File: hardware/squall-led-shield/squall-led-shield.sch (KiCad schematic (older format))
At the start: 10 parts, among them J1 SQUALL_HEADER, Q1 Q_2NMOS

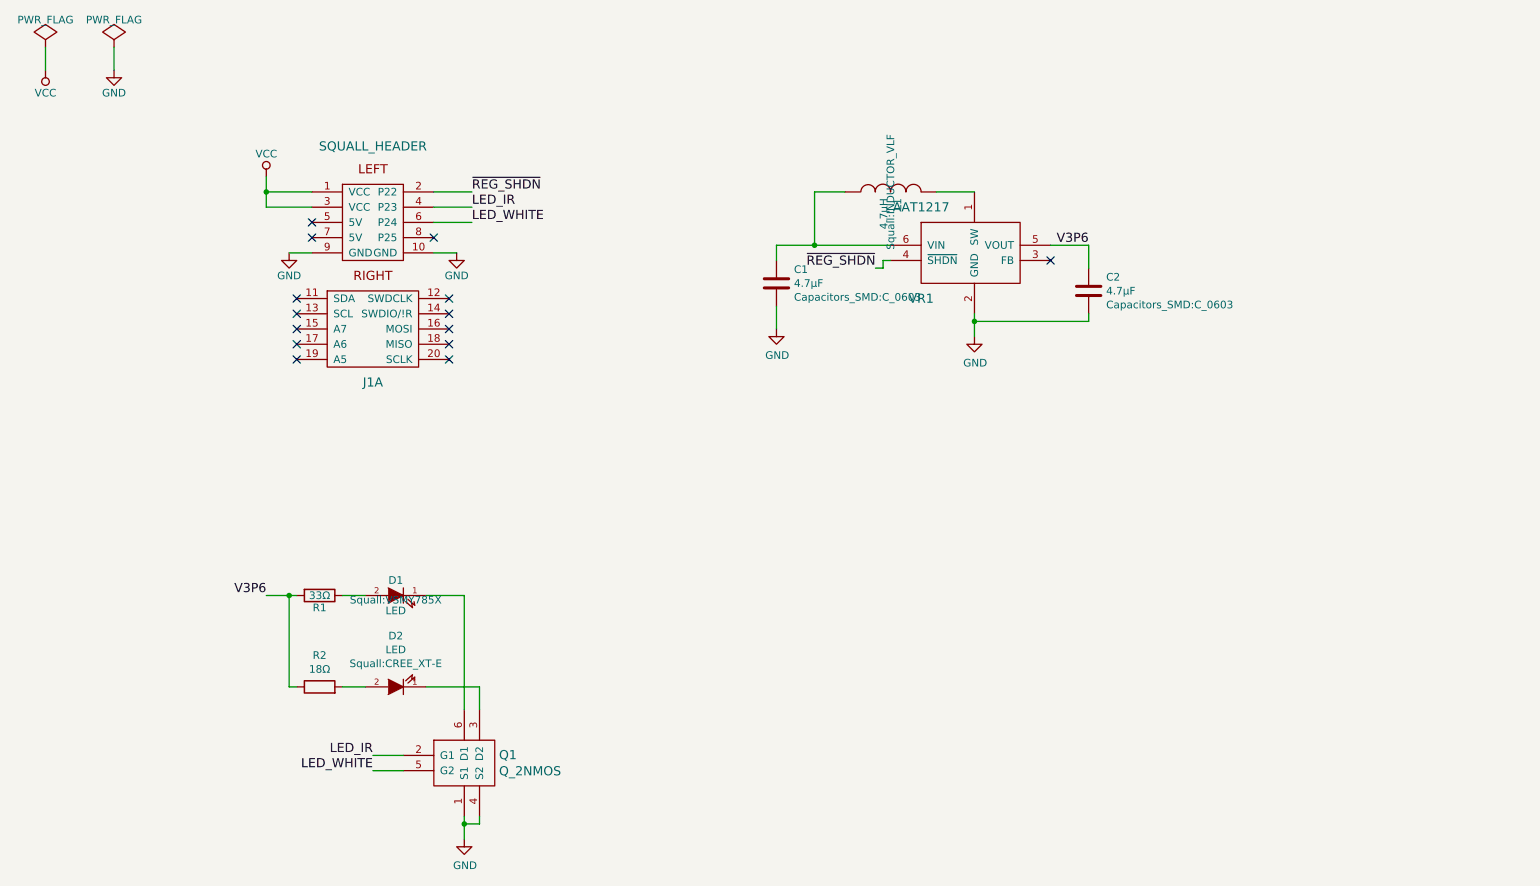
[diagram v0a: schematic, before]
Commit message: WIP: Add explicit thermal pin
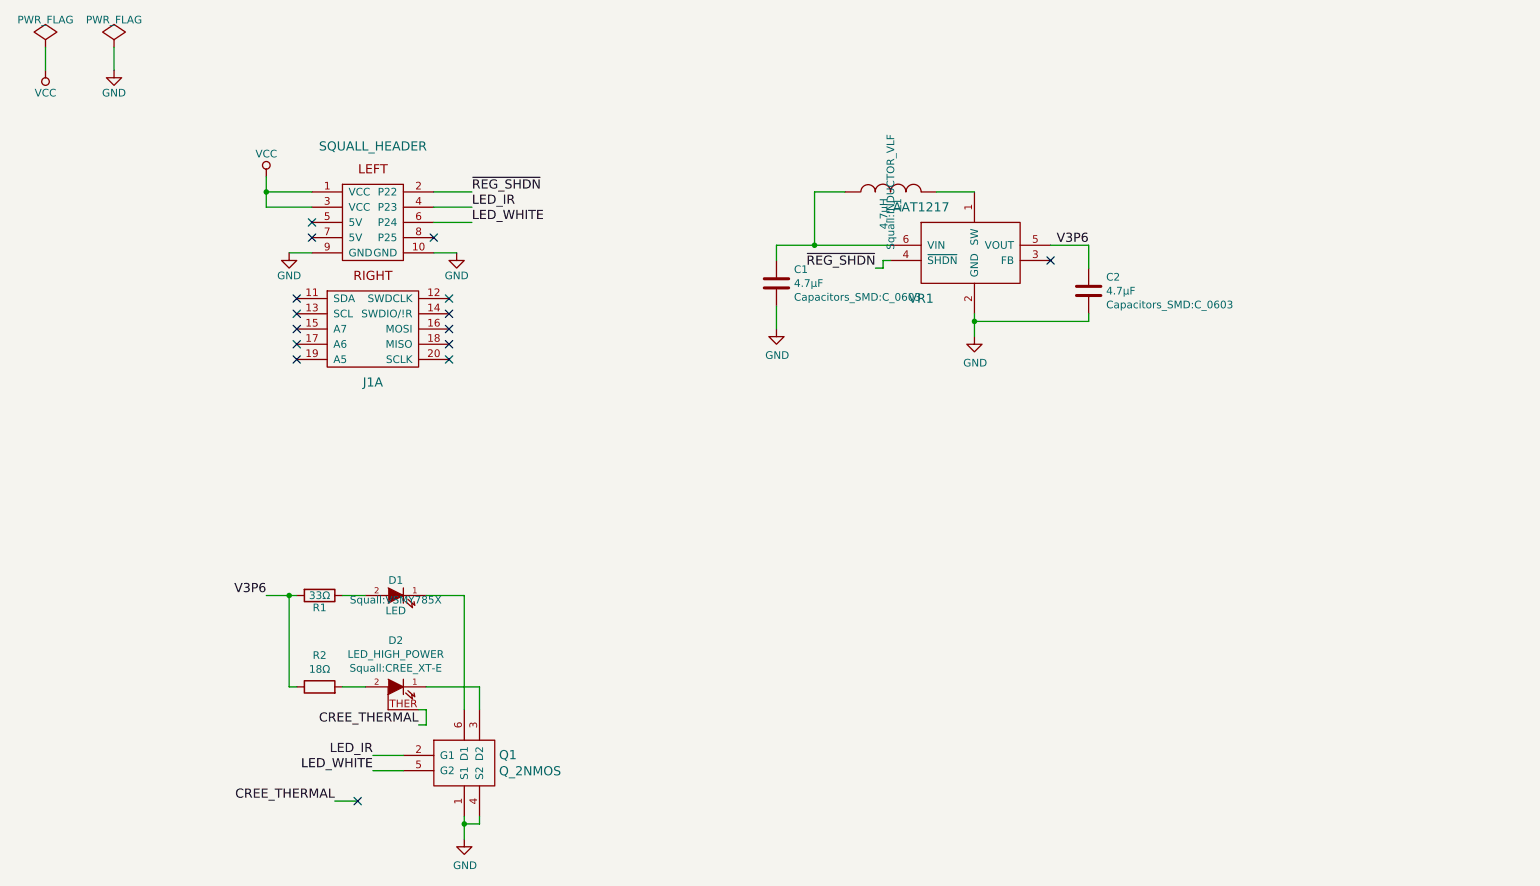
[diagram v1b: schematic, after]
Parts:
- removed D2: LED, Squall:CREE_XT-E, symbol LED
- added D2: LED_HIGH_POWER, Squall:CREE_XT-E, symbol LED_HIGH_POWER
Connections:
- net at R2.2: now also D2.2 (A)
- net at Q1.3 (D2): now also D2.1 (K)
- new net CREE_THERMAL: D2.THER (THERMAL)
- no-connect marks 14 -> 15
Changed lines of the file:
@@
 	5550 2650 5550 2500
 Wire Wire Line
-	6300 2100 5550 2100
+	5550 2100 6300 2100
 Wire Wire Line
 	5550 2100 5550 2200
@@
 	1    2550 5000
 	0    -1   -1   0
-$EndComp
-$Comp
-L LED D2
-U 1 1 5792A13B
-P 3050 5000
-F 0 "D2" H 3050 4665 50  0000 C CNN
-F 1 "LED" H 3050 4756 50  0000 C CNN
-F 2 "Squall:CREE_XT-E" H 3050 4847 50  0000 C CNN
-F 3 "" H 3050 5000 50  0000 C CNN
-	1    3050 5000
-	-1   0    0    1
 $EndComp
 Wire Wire Line
@@
 $EndComp
 Wire Wire Line
-	3500 6000 3500 5850
+	3500 5850 3500 6000
 Wire Wire Line
 	3500 5900 3600 5900
@@
 ~REG_SHDN
 Wire Wire Line
-	2400 4400 2200 4400
+	2200 4400 2400 4400
 Wire Wire Line
 	2350 4400 2350 5000
@@
 Text Label 2900 5550 2    60   ~ 0
 LED_WHITE
+$Comp
+L LED_HIGH_POWER D2
+U 1 1 579524D4
+P 3050 5000
+F 0 "D2" H 3050 5305 50  0000 C CNN
+F 1 "LED_HIGH_POWER" H 3050 5214 50  0000 C CNN
+F 2 "Squall:CREE_XT-E" H 3050 5123 50  0000 C CNN
+F 3 "" H 3050 5000 50  0000 C CNN
+	1    3050 5000
+	-1   0    0    -1
+$EndComp
+Text Label 3200 5250 2    60   ~ 0
+CREE_THERMAL
+Wire Wire Line
+	3250 5150 3250 5250
+Wire Wire Line
+	3250 5250 3200 5250
+Wire Wire Line
+	3200 5150 3250 5150
+Wire Wire Line
+	2650 5750 2800 5750
+Text Label 2650 5750 2    60   ~ 0
+CREE_THERMAL
+NoConn ~ 2800 5750
 $EndSCHEMATC

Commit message: WIP: Tie regulator to VCC
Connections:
- net VCC: now also C1.1, L1.1, VR1.6 (VIN)
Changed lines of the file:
@@
 	5550 2650 5550 2500
 Wire Wire Line
-	5550 2100 6300 2100
+	5400 2100 6300 2100
 Wire Wire Line
 	5550 2100 5550 2200
@@
 CREE_THERMAL
 NoConn ~ 2800 5750
+Text Label 5400 2100 2    60   ~ 0
+VCC
+Connection ~ 5550 2100
 $EndSCHEMATC

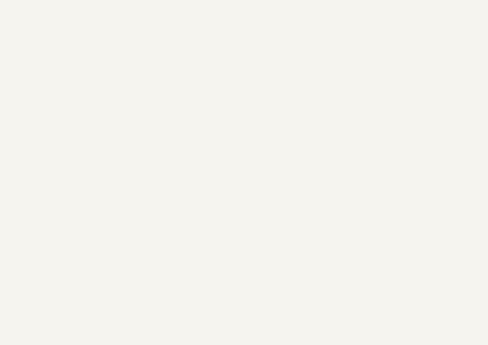
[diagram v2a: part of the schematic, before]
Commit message: Add CubeWorks logo
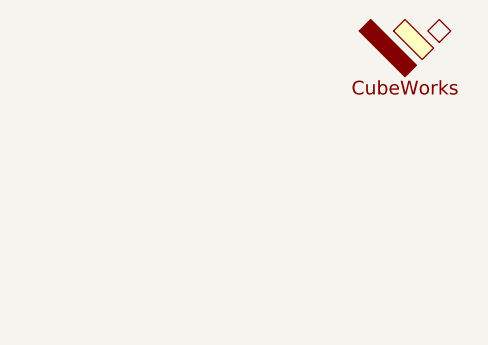
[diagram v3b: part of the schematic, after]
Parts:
- added _1: CubeWorks-Logo, Squall:CubeWorks_Logo-5mm, symbol CubeWorks-Logo
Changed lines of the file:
@@
 VCC
 Connection ~ 5550 2100
+$Comp
+L CubeWorks-Logo _1
+U 1 1 579536BF
+P 10200 700
+F 0 "_1" H 10200 900 60  0001 C CNN
+F 1 "CubeWorks-Logo" H 10200 1000 60  0001 C CNN
+F 2 "Squall:CubeWorks_Logo-5mm" H 10225 825 60  0001 C CNN
+F 3 "" H 10225 825 60  0001 C CNN
+	1    10200 700
+	1    0    0    -1
+$EndComp
 $EndSCHEMATC
